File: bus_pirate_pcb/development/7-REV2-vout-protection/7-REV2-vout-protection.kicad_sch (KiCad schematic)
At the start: 11 parts

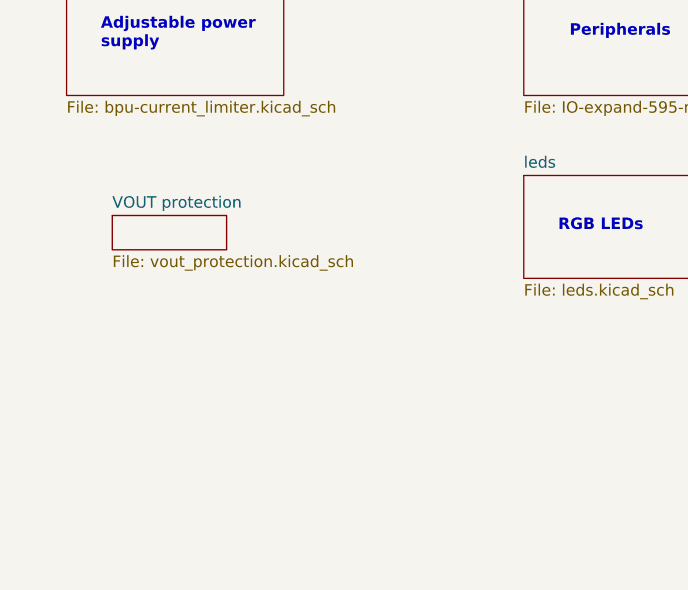
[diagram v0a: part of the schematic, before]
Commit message: BP 7R2 VOUT protection
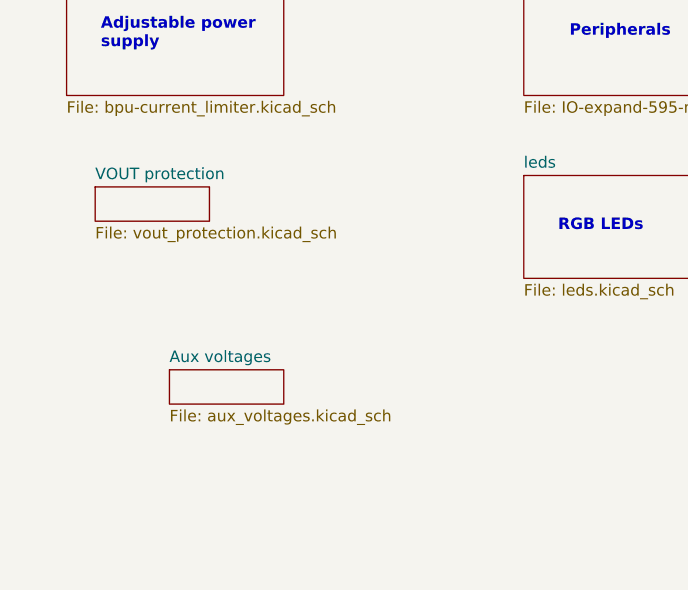
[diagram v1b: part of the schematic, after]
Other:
- added sheet Aux voltages (aux_voltages.kicad_sch)
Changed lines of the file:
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@@
 	)
 	(sheet
-		(at 26.67 51.435)
+		(at 24.765 48.26)
 		(size 12.7 3.81)
 		(exclude_from_sim no)
@@
 		)
 		(property "Sheetname" "VOUT protection"
-			(at 26.67 50.7234 0)
+			(at 24.765 47.5484 0)
 			(effects
 				(font
@@
 		)
 		(property "Sheetfile" "vout_protection.kicad_sch"
-			(at 26.67 55.8296 0)
+			(at 24.765 52.6546 0)
 			(effects
 				(font
@@
 			(project "7-REV2-vout-protection"
 				(path "/1f56410a-eaac-4444-b0f7-cfd3531e22ac"
-					(page "8")
+					(page "9")
 				)
 			)
+		)
+	)
+	(sheet
+		(at 33.02 68.58)
+		(size 12.7 3.81)
+		(exclude_from_sim no)
+		(in_bom yes)
+		(on_board yes)
+		(dnp no)
+		(fields_autoplaced yes)
+		(stroke
+			(width 0.1524)
+			(type solid)
+		)
+		(fill
+			(color 0 0 0 0.0000)
+		)
+		(property "Sheetname" "Aux voltages"
+			(at 33.02 67.8684 0)
+			(effects
+				(font
+					(size 1.27 1.27)
+				)
+				(justify left bottom)
+			)
+		)
+		(property "Sheetfile" "aux_voltages.kicad_sch"
+			(at 33.02 72.9746 0)
+			(effects
+				(font
+					(size 1.27 1.27)
+				)
+				(justify left top)
+			)
+		)
+		(instances
+			(project "7-REV2-vout-protection"
+				(path "/1f56410a-eaac-4444-b0f7-cfd3531e22ac"
+					(page "9")
+				)
+			)

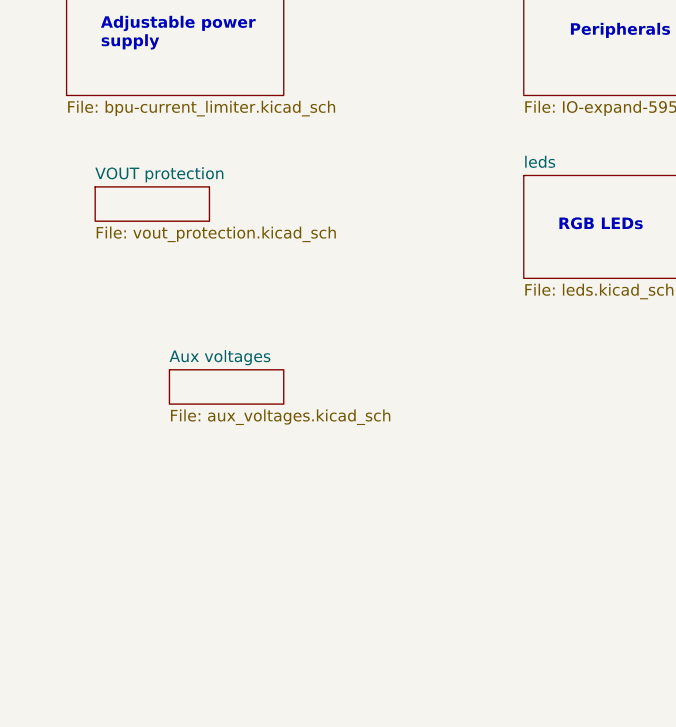
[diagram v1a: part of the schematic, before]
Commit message: 7R2 with vout protection
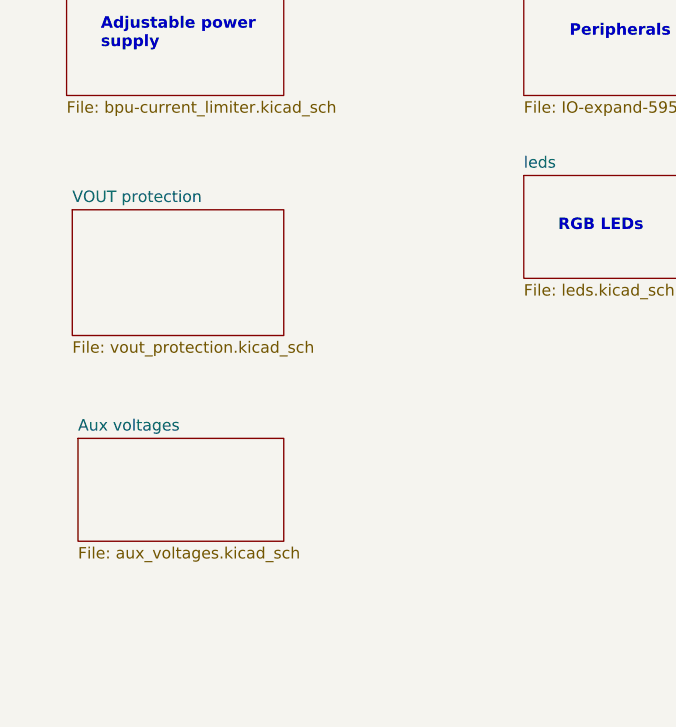
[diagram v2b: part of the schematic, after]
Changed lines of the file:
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@@
 	)
 	(sheet
-		(at 24.765 48.26)
-		(size 12.7 3.81)
+		(at 22.225 50.8)
+		(size 23.495 13.97)
 		(exclude_from_sim no)
 		(in_bom yes)
@@
 		)
 		(property "Sheetname" "VOUT protection"
-			(at 24.765 47.5484 0)
+			(at 22.225 50.0884 0)
 			(effects
 				(font
@@
 		)
 		(property "Sheetfile" "vout_protection.kicad_sch"
-			(at 24.765 52.6546 0)
+			(at 22.225 65.3546 0)
 			(effects
 				(font
@@
 	)
 	(sheet
-		(at 33.02 68.58)
-		(size 12.7 3.81)
+		(at 22.86 76.2)
+		(size 22.86 11.43)
 		(exclude_from_sim no)
 		(in_bom yes)
@@
 		)
 		(property "Sheetname" "Aux voltages"
-			(at 33.02 67.8684 0)
+			(at 22.86 75.4884 0)
 			(effects
 				(font
@@
 		)
 		(property "Sheetfile" "aux_voltages.kicad_sch"
-			(at 33.02 72.9746 0)
+			(at 22.86 88.2146 0)
 			(effects
 				(font
